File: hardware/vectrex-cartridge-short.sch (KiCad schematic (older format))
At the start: 15 parts, among them CON1 vectrex-edge-connector, SW1 SW_DIP_x03, U1 AT27C256R-70PU / AT27C512R-70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, U2 DS2431+ TO-92

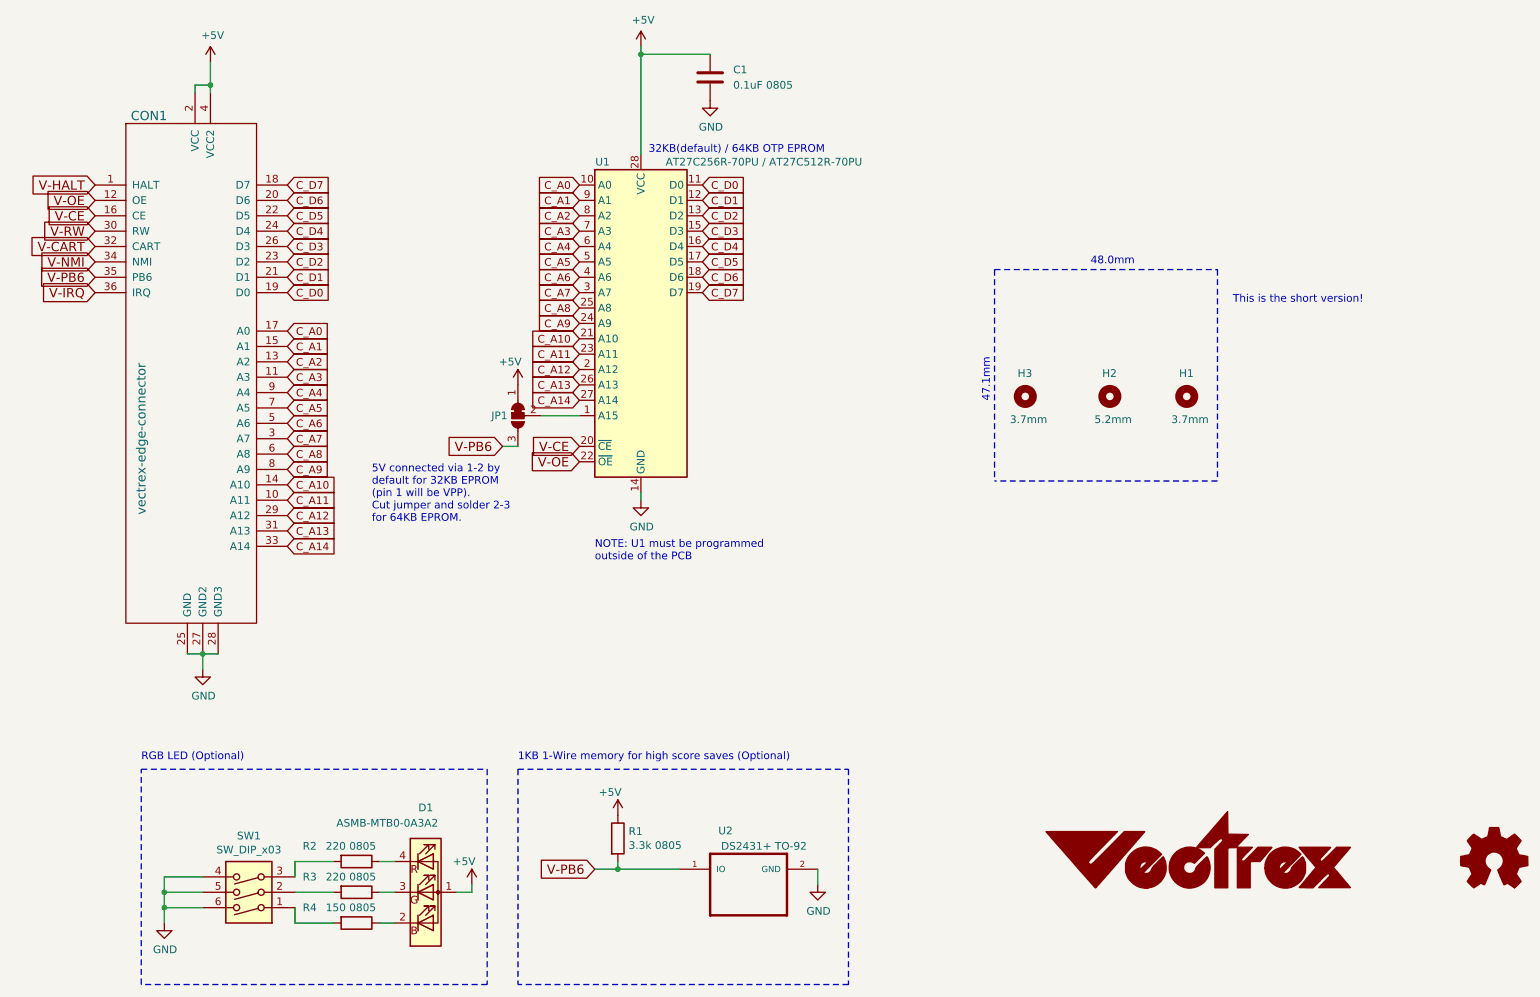
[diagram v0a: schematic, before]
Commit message: added RGB LED to Vectrex Cartridge v1.1, also added stand-alone LED PCB v1.0
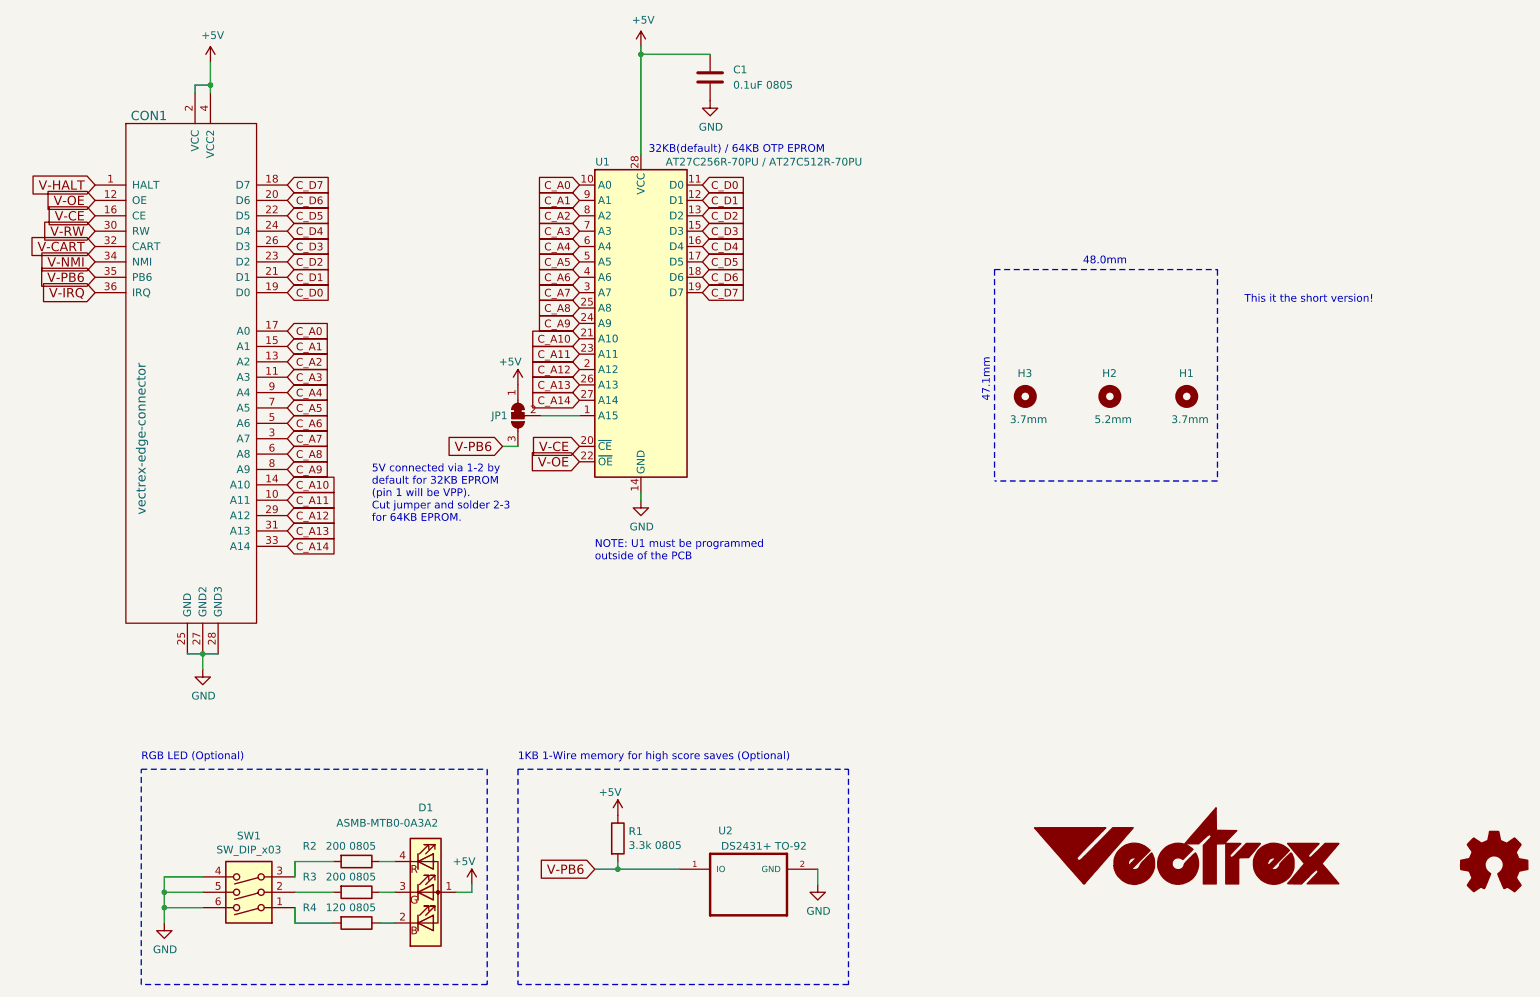
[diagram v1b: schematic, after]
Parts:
- G1: footprint vectrex-cartridge:vectrex-us-soldermask-15mm -> vectrex-cartridge:vectrex-us-soldermask-37mm
- R2, R3: value 220 0805 -> 200 0805
- R4: value 150 0805 -> 120 0805
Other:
- note added: "This it the short version!"
- note removed: "This is the short version!"
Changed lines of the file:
@@
 L Graphic:Logo_Open_Hardware_Small #LOGO1
 U 1 1 5EE7732D
-P 10950 6900
-F 0 "#LOGO1" H 10950 7175 50  0001 C CNN
-F 1 "Logo_Open_Hardware_Small" H 10950 6675 50  0001 C CNN
-F 2 "" H 10950 6900 50  0001 C CNN
-F 3 "~" H 10950 6900 50  0001 C CNN
-	1    10950 6900
+P 10950 6925
+F 0 "#LOGO1" H 10950 7200 50  0001 C CNN
+F 1 "Logo_Open_Hardware_Small" H 10950 6700 50  0001 C CNN
+F 2 "" H 10950 6925 50  0001 C CNN
+F 3 "~" H 10950 6925 50  0001 C CNN
+	1    10950 6925
 	1    0    0    -1
 $EndComp
@@
 Wire Notes Line style solid
 	7700 3050 7700 4425
-Text Notes 8325 3025 0    50   ~ 0
+Text Notes 8275 3025 0    50   ~ 0
 48.0mm
 Text Notes 7675 3625 3    50   ~ 0
 47.1mm\n
+Text Notes 9325 3275 0    50   ~ 0
+This it the short version!
 Text GLabel 5800 3200 2    50   Input ~ 0
 C_D7
@@
 L vectrex-us:LOGO G1
 U 1 1 5EF1F12E
-P 9025 6825
-F 0 "G1" H 9025 6605 60  0001 C CNN
-F 1 "LOGO" H 9025 7045 60  0001 C CNN
-F 2 "vectrex-cartridge:vectrex-us-soldermask-15mm" H 9025 6825 50  0001 C CNN
-F 3 "" H 9025 6825 50  0001 C CNN
-	1    9025 6825
+P 8950 6800
+F 0 "G1" H 8950 6580 60  0001 C CNN
+F 1 "LOGO" H 8950 7020 60  0001 C CNN
+F 2 "vectrex-cartridge:vectrex-us-soldermask-37mm" H 8950 6800 50  0001 C CNN
+F 3 "" H 8950 6800 50  0001 C CNN
+	1    8950 6800
 	1    0    0    -1
 $EndComp
@@
 P 3550 6900
 F 0 "R2" V 3450 6550 50  0000 L CNN
-F 1 "220 0805" V 3450 6700 50  0000 L CNN
+F 1 "200 0805" V 3450 6700 50  0000 L CNN
 F 2 "Resistor_SMD:R_0805_2012Metric_Pad1.15x1.40mm_HandSolder" V 3480 6900 50  0001 C CNN
 F 3 "~" H 3550 6900 50  0001 C CNN
@@
 P 3550 7100
 F 0 "R3" V 3450 6750 50  0000 L CNN
-F 1 "220 0805" V 3450 6900 50  0000 L CNN
+F 1 "200 0805" V 3450 6900 50  0000 L CNN
 F 2 "Resistor_SMD:R_0805_2012Metric_Pad1.15x1.40mm_HandSolder" V 3480 7100 50  0001 C CNN
 F 3 "~" H 3550 7100 50  0001 C CNN
@@
 P 3550 7300
 F 0 "R4" V 3450 6950 50  0000 L CNN
-F 1 "150 0805" V 3450 7100 50  0000 L CNN
+F 1 "120 0805" V 3450 7100 50  0000 L CNN
 F 2 "Resistor_SMD:R_0805_2012Metric_Pad1.15x1.40mm_HandSolder" V 3480 7300 50  0001 C CNN
 F 3 "~" H 3550 7300 50  0001 C CNN
@@
 Wire Wire Line
 	3150 7300 3400 7300
-Text Notes 9250 3275 0    50   ~ 0
-This is the short version!
 $EndSCHEMATC

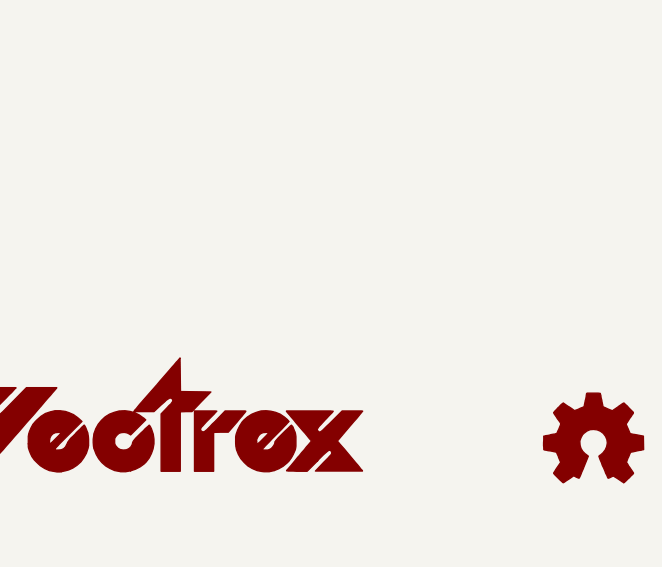
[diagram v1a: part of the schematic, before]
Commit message: Updated DS2431 footprint, and many little tweaks for v1.2
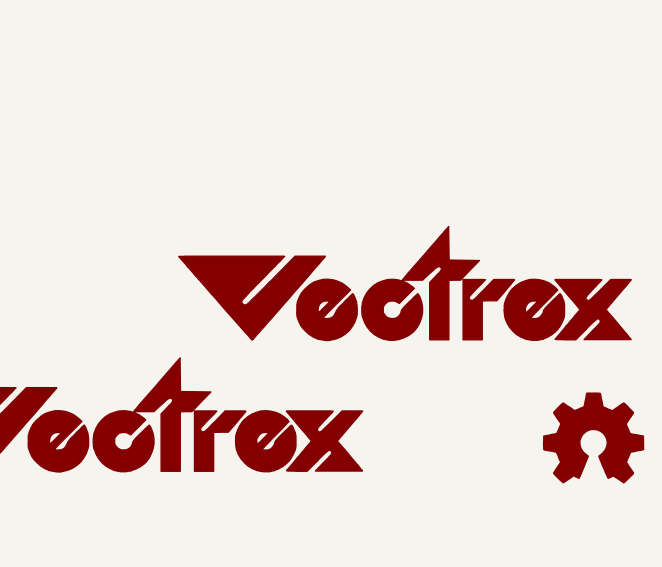
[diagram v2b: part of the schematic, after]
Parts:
- added G2: LOGO, vectrex-cartridge:vectrex-us-soldermask-15mm, symbol vectrex-us:LOGO
- U2: footprint vectrex-cartridge:TO-92L_HandSolder -> vectrex-cartridge:TO-92_Inline_BW
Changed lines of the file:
@@
 Sheet 1 1
 Title "Vectrex Cartridge"
-Date "2020-06-28"
-Rev "v1.1"
+Date "2020-07-05"
+Rev "v1.2"
 Comp "Brett Walach"
 Comment1 ""
@@
 F 0 "U2" H 5950 7400 50  0000 C CNN
 F 1 "DS2431+ TO-92" H 6200 7300 50  0000 C CNN
-F 2 "vectrex-cartridge:TO-92L_HandSolder" H 5850 7050 50  0001 C CNN
+F 2 "vectrex-cartridge:TO-92_Inline_BW" H 5850 7050 50  0001 C CNN
 F 3 "" H 5850 7050 50  0001 C CNN
 	1    5850 7050
@@
 Wire Wire Line
 	3150 7300 3400 7300
+$Comp
+L vectrex-us:LOGO G2
+U 1 1 5F02F273
+P 10125 6225
+F 0 "G2" H 10125 6005 60  0001 C CNN
+F 1 "LOGO" H 10125 6445 60  0001 C CNN
+F 2 "vectrex-cartridge:vectrex-us-soldermask-15mm" H 10125 6225 50  0001 C CNN
+F 3 "" H 10125 6225 50  0001 C CNN
+	1    10125 6225
+	1    0    0    -1
+$EndComp
 $EndSCHEMATC
